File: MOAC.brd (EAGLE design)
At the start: 113 x 40 mm, 56 parts, among them IC1 ATMEGA32U4NT-TQFP, J1 3.5mm, J2 3.5mm, J3 3.5mm, J4 3.5mm, J5 3.5mm, J6 3.5mm, J7 3.5mm, J8 3.5mm, J9 USB-C

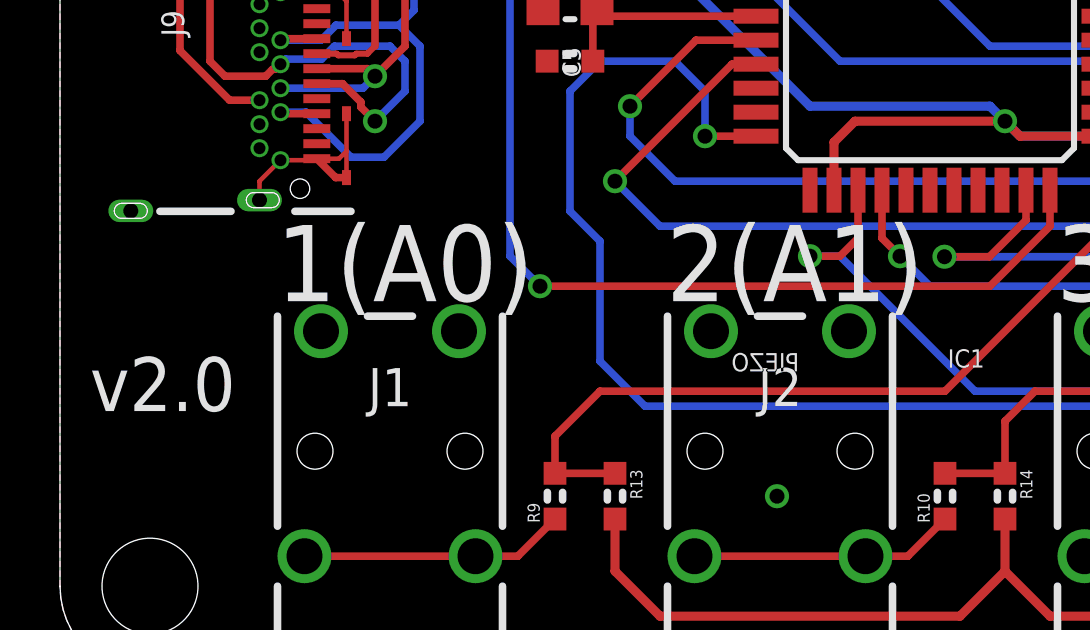
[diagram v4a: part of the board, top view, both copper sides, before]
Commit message: Changed button 8 from A11 to A7, to fix Jon's silly mistake from way back in v1.0
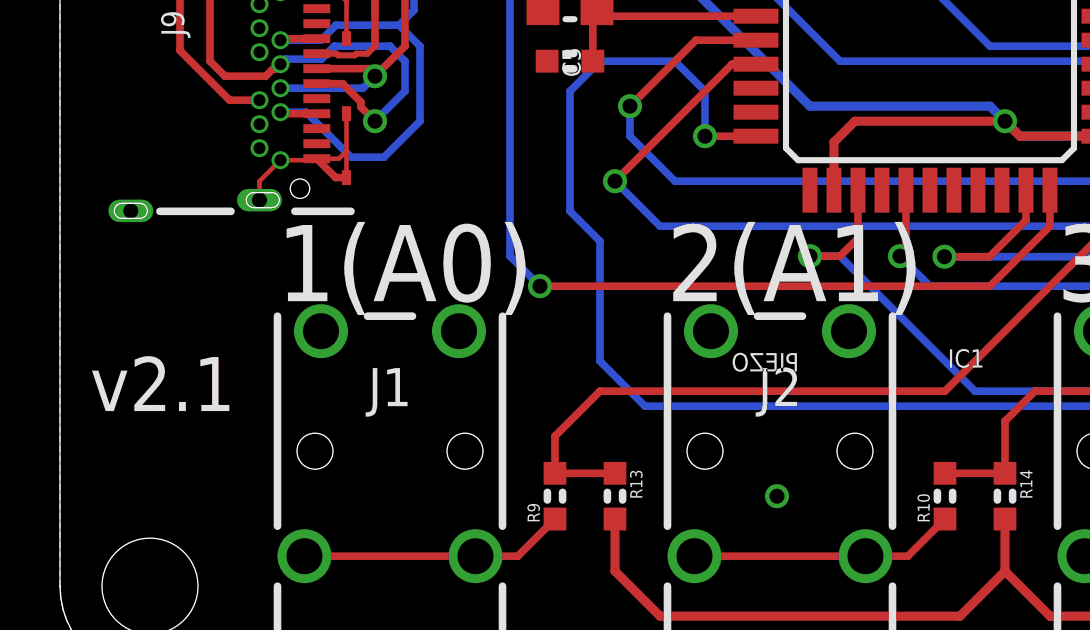
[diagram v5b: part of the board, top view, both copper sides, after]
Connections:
- net D10_A11 renamed D10_A10
- net D8_A9 renamed D8_A8
- net D9_A10 renamed D9_A9
- removed net D12_A7: IC1.26, R21.2, R25.1
- removed net D6_A8: IC1.27
- new net D12_A11: IC1.26
- new net D6_A7: IC1.27, R21.2, R25.1
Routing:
- net D12_A7: track 87.6 -> 0.00 mm, vias 2 -> 0
- net D6_A7: track 0.00 -> 87.4 mm, vias 0 -> 2
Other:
- board text added: "v2.1"
- board text removed: "v2.0"
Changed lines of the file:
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@@
 <drawing>
 <settings>
-<setting alwaysvectorfont="yes"/>
+<setting alwaysvectorfont="no"/>
 <setting keepoldvectorfont="yes"/>
 <setting verticaltext="up"/>
 </settings>
-<grid distance="1" unitdist="mm" unit="mm" style="dots" multiple="1" display="yes" altdistance="0.001" altunitdist="inch" altunit="inch"/>
+<grid distance="0.5" unitdist="mm" unit="mm" style="dots" multiple="1" display="yes" altdistance="0.001" altunitdist="inch" altunit="inch"/>
 <layers>
 <layer number="1" name="Top" color="4" fill="1" visible="yes" active="yes"/>
@@
 <layer number="20" name="Dimension" color="15" fill="1" visible="yes" active="yes"/>
 <layer number="21" name="tPlace" color="7" fill="1" visible="yes" active="yes"/>
-<layer number="22" name="bPlace" color="14" fill="1" visible="yes" active="yes"/>
+<layer number="22" name="bPlace" color="14" fill="1" visible="no" active="yes"/>
 <layer number="23" name="tOrigins" color="15" fill="1" visible="yes" active="yes"/>
 <layer number="24" name="bOrigins" color="15" fill="1" visible="yes" active="yes"/>
@@
 </layers>
 <board>
-<fusionsync huburn="a.cGVyc29uYWw6dWUyZDliZmNi" projecturn="a.cGVyc29uYWw6dWUyZDliZmNiIzIwMTgxMTA5MTU5MjczMjgx" f3durn="urn:adsk.wipprod:dm.lineage:ugFpkX5gRSuWYfeIfJSr2A" pcbguid="4ef23d0d-506b-4405-99bc-0b8b5e44c8a7" lastpulledtime="" lastsyncedchangeguid="f2f5a112-46de-bc3b-63a8-23ca9d30e68b"/>
+<fusionsync huburn="a.cGVyc29uYWw6dWUyZDliZmNi" projecturn="a.cGVyc29uYWw6dWUyZDliZmNiIzIwMTgxMTA5MTU5MjczMjgx" f3durn="urn:adsk.wipprod:dm.lineage:ugFpkX5gRSuWYfeIfJSr2A" pcbguid="4ef23d0d-506b-4405-99bc-0b8b5e44c8a7" lastpulledtime="" lastsyncedchangeguid="1a155890-40f8-0c29-352a-23eae3b4c9ee"/>
 <plain>
 <wire x1="113" y1="3" x2="113" y2="37" width="0" layer="20"/>
@@
 <text x="44.958" y="14.224" size="0.6096" layer="25">LED1</text>
 <text x="44.958" y="4.572" size="0.6096" layer="25">LED2</text>
-<text x="1" y="8.8364" size="1.8" layer="21" font="vector" ratio="15">v2.0</text>
+<text x="1" y="8.8364" size="1.8" layer="21" font="vector" ratio="15">v2.1</text>
 <hole x="3" y="3" drill="3.2"/>
 <hole x="3" y="37" drill="3.2"/>
@@
 <element name="C2" library="SuperHouse-DiscreteSemi" library_urn="urn:adsk.eagle:library:11768461" package="C0603" package3d_urn="urn:adsk.eagle:package:7066315/6" value="100nF" x="37" y="30" smashed="yes" rot="R270">
 <attribute name="NAME" x="37.4826" y="30.2794" size="0.6096" layer="25" font="vector" rot="R180"/>
-<attribute name="VALUE" x="35.984" y="31.357" size="0.8128" layer="27" font="vector"/>
+<attribute name="VALUE" x="37.984" y="29.357" size="0.8128" layer="27" font="vector"/>
 </element>
 <element name="R2" library="SuperHouse-DiscreteSemi" library_urn="urn:adsk.eagle:library:11768461" package="R0603" package3d_urn="urn:adsk.eagle:package:11768543/2" value="10K" x="20.5" y="27" smashed="yes" rot="R270">
 <attribute name="NAME" x="20.9064" y="27.2793" size="0.6096" layer="25" font="vector" rot="R180"/>
-<attribute name="VALUE" x="20.1431" y="25.984" size="0.8128" layer="27" font="vector" rot="R90"/>
+<attribute name="VALUE" x="17.984" y="27.8569" size="0.8128" layer="27" font="vector"/>
 </element>
 <element name="C3" library="SuperHouse-DiscreteSemi" library_urn="urn:adsk.eagle:library:11768461" package="C0603" package3d_urn="urn:adsk.eagle:package:7066315/6" value="1uF" x="12" y="34" smashed="yes" rot="R180">
@@
 <element name="C1" library="SuperHouse-DiscreteSemi" library_urn="urn:adsk.eagle:library:11768461" package="C0603" package3d_urn="urn:adsk.eagle:package:7066315/6" value="100nF" x="37" y="26" smashed="yes" rot="R90">
 <attribute name="NAME" x="36.5174" y="25.7206" size="0.6096" layer="25" font="vector"/>
-<attribute name="VALUE" x="36.484" y="23.857" size="0.8128" layer="27" font="vector"/>
+<attribute name="VALUE" x="37.484" y="26.857" size="0.8128" layer="27" font="vector"/>
 </element>
 <element name="ICSP" library="SuperHouse-Connectors" library_urn="urn:adsk.eagle:library:11765989" package="2X03PTH" package3d_urn="urn:adsk.eagle:package:11765966/5" value="ICSP" x="32.7036" y="36.64" smashed="yes">
@@
 <element name="Z2" library="SuperHouse-DiscreteSemi" library_urn="urn:adsk.eagle:library:11768461" package="TVS0603" package3d_urn="urn:adsk.eagle:package:11801346/2" value="PGB1010603" x="28.5" y="31" smashed="yes" rot="R90">
 <attribute name="NAME" x="28.754" y="30.619" size="0.4064" layer="25" font="vector" rot="R90"/>
-<attribute name="VALUE" x="28.4652" y="32.484" size="0.8128" layer="27" font="vector" rot="R90"/>
+<attribute name="VALUE" x="27.9652" y="28.984" size="0.8128" layer="27" font="vector" rot="R90"/>
 </element>
 <element name="C5" library="SuperHouse-DiscreteSemi" library_urn="urn:adsk.eagle:library:11768461" package="C0603" package3d_urn="urn:adsk.eagle:package:7066315/6" value="15pF" x="17" y="20.5" smashed="yes">
@@
 <element name="C4" library="SuperHouse-DiscreteSemi" library_urn="urn:adsk.eagle:library:11768461" package="C0603" package3d_urn="urn:adsk.eagle:package:7066315/6" value="1uF" x="25.5" y="31" smashed="yes" rot="R270">
 <attribute name="NAME" x="24.9666" y="30.7206" size="0.6096" layer="25" font="vector"/>
-<attribute name="VALUE" x="24.484" y="30.5348" size="0.8128" layer="27" font="vector"/>
+<attribute name="VALUE" x="23.984" y="30.5348" size="0.8128" layer="27" font="vector"/>
 </element>
 <element name="XTL1" library="SuperHouse-Oscillators" library_urn="urn:adsk.eagle:library:11786724" package="CRYSTAL-SMD-3X2" package3d_urn="urn:adsk.eagle:package:7066259/2" value="16MHz" x="17" y="23.5" smashed="yes" rot="R270">
@@
 <element name="R1" library="SuperHouse-DiscreteSemi" library_urn="urn:adsk.eagle:library:11768461" package="R0603" package3d_urn="urn:adsk.eagle:package:11768543/2" value="22R" x="32.5" y="31" smashed="yes" rot="R270">
 <attribute name="NAME" x="33.008" y="31.889" size="0.4064" layer="25" font="vector" rot="R270"/>
-<attribute name="VALUE" x="31.484" y="32.5348" size="0.8128" layer="27" font="vector"/>
+<attribute name="VALUE" x="31.484" y="30.5348" size="0.8128" layer="27" font="vector"/>
 </element>
 <element name="R6" library="SuperHouse-DiscreteSemi" library_urn="urn:adsk.eagle:library:11768461" package="R0603" package3d_urn="urn:adsk.eagle:package:11768543/2" value="22R" x="30.5" y="31" smashed="yes" rot="R270">
 <attribute name="NAME" x="31.008" y="31.889" size="0.4064" layer="25" font="vector" rot="R270"/>
-<attribute name="VALUE" x="29.484" y="30.5348" size="0.8128" layer="27" font="vector"/>
+<attribute name="VALUE" x="29.484" y="32.0348" size="0.8128" layer="27" font="vector"/>
 </element>
 <element name="S10" library="SuperHouse-Switches" library_urn="urn:adsk.eagle:library:11744182" package="TACTILE_SMD_3X4X2" package3d_urn="urn:adsk.eagle:package:11818379/3" value="HWB" x="9" y="37" smashed="yes" rot="R180"/>
@@
 <attribute name="VALUE" x="47.28" y="22.215" size="1.27" layer="27"/>
 </element>
-<element name="IC1" library="SuperHouse-MCUs" library_urn="urn:adsk.eagle:library:11815114" package="TQFP44" package3d_urn="urn:adsk.eagle:package:12190647/2" value="ATMEGA32U4NT-TQFP" x="29" y="22" smashed="yes" rot="R270">
+<element name="IC1" library="SuperHouse-MCUs" library_urn="urn:adsk.eagle:library:11815114" package="TQFP44" package3d_urn="urn:adsk.eagle:package:12190647/3" value="ATMEGA32U4NT-TQFP" x="29" y="22" smashed="yes" rot="R270">
 <attribute name="NAME" x="35.985" y="25.81" size="1.778" layer="25" rot="R270"/>
-<attribute name="VALUE" x="20.2449" y="26.445" size="1.778" layer="27" rot="R270"/>
+<attribute name="VALUE" x="24.555" y="19.2449" size="0.8128" layer="27"/>
 </element>
 </elements>
@@
 <wire x1="106.762" y1="25" x2="109.238" y2="25" width="0.254" layer="1"/>
 </signal>
-<signal name="D12_A7">
-<contactref element="R21" pad="2"/>
-<contactref element="R25" pad="1"/>
-<wire x1="109.5" y1="9.762" x2="107.5" y2="9.762" width="0.254" layer="1"/>
-<via x="28" y="14" extent="1-16" drill="0.5"/>
-<wire x1="28" y1="14" x2="29" y2="13" width="0.254" layer="16"/>
-<via x="107.5" y="13" extent="1-16" drill="0.5"/>
-<wire x1="107.5" y1="13" x2="107.5" y2="9.762" width="0.254" layer="1"/>
-<wire x1="29" y1="13" x2="107.5" y2="13" width="0.254" layer="16"/>
-<contactref element="IC1" pad="26"/>
-<wire x1="27.4" y1="16.2" x2="27.4" y2="14.6" width="0.254" layer="1"/>
-<wire x1="27.4" y1="14.6" x2="28" y2="14" width="0.254" layer="1"/>
-</signal>
 <signal name="D4_A6">
 <contactref element="R20" pad="2"/>
@@
 <contactref element="IC1" pad="21"/>
 </signal>
-<signal name="D6_A8">
+<signal name="D6_A7">
 <contactref element="IC1" pad="27"/>
-</signal>
-<signal name="D8_A9">
+<contactref element="R21" pad="2"/>
+<contactref element="R25" pad="1"/>
+<wire x1="109.5" y1="9.762" x2="107.5" y2="9.762" width="0.254" layer="1"/>
+<via x="28" y="14" extent="1-16" drill="0.5"/>
+<wire x1="28" y1="14" x2="29" y2="13" width="0.254" layer="16"/>
+<via x="107.5" y="13" extent="1-16" drill="0.5"/>
+<wire x1="107.5" y1="13" x2="107.5" y2="9.762" width="0.254" layer="1"/>
+<wire x1="29" y1="13" x2="107.5" y2="13" width="0.254" layer="16"/>
+<wire x1="28.2" y1="16.2" x2="28.2" y2="14.2" width="0.254" layer="1"/>
+<wire x1="28.2" y1="14.2" x2="28" y2="14" width="0.254" layer="1"/>
+</signal>
+<signal name="D8_A8">
 <contactref element="IC1" pad="28"/>
 </signal>
-<signal name="D9_A10">
+<signal name="D9_A9">
 <contactref element="IC1" pad="29"/>
 </signal>
-<signal name="D10_A11">
+<signal name="D10_A10">
 <contactref element="IC1" pad="30"/>
 </signal>
+<signal name="D12_A11">
+<contactref element="IC1" pad="26"/>
+</signal>
 </signals>

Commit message: Changed display from 128x32 to 128x64
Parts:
- MOD2: value OLED-I2C128X64-1.3-HO -> OLED-I2C128X64-1.3-5.08; device SuperHouse-Displays:OLED-128X64-1.3-HO -> SuperHouse-Displays:OLED-128X64-1.3-5.08
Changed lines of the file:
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@@
 <?xml version="1.0" encoding="utf-8"?>
 <!DOCTYPE eagle SYSTEM "eagle.dtd">
-<eagle version="9.4.2">
+<eagle version="9.5.2">
 <drawing>
 <settings>
@@
 </layers>
 <board>
-<fusionsync huburn="a.cGVyc29uYWw6dWUyZDliZmNi" projecturn="a.cGVyc29uYWw6dWUyZDliZmNiIzIwMTgxMTA5MTU5MjczMjgx" f3durn="urn:adsk.wipprod:dm.lineage:ugFpkX5gRSuWYfeIfJSr2A" pcbguid="4ef23d0d-506b-4405-99bc-0b8b5e44c8a7" lastpulledtime="" lastsyncedchangeguid="1a155890-40f8-0c29-352a-23eae3b4c9ee"/>
+<fusionsync huburn="a.cGVyc29uYWw6dWUyZDliZmNi" projecturn="a.cGVyc29uYWw6dWUyZDliZmNiIzIwMTgxMTA5MTU5MjczMjgx" f3durn="urn:adsk.wipprod:dm.lineage:ugFpkX5gRSuWYfeIfJSr2A" pcbguid="4ef23d0d-506b-4405-99bc-0b8b5e44c8a7" lastpulledtime="" lastsyncedchangeguid="8fe81872-e2fd-63fb-760c-4497a8ebff07"/>
 <plain>
 <wire x1="113" y1="3" x2="113" y2="37" width="0" layer="20"/>
@@
 <attribute name="VALUE" x="17.984" y="7.5348" size="0.8128" layer="27" font="vector"/>
 </element>
-<element name="MOD2" library="SuperHouse-Displays" library_urn="urn:adsk.eagle:library:11966779" package="OLED-128X64-1.3-HO" package3d_urn="urn:adsk.eagle:package:12058301/2" value="OLED-I2C128X64-1.3-HO" x="56.5" y="20" smashed="yes">
+<element name="MOD2" library="SuperHouse-Displays" library_urn="urn:adsk.eagle:library:11966779" package="OLED-128X64-1.3-5.08" package3d_urn="urn:adsk.eagle:package:16152188/2" value="OLED-I2C128X64-1.3-5.08" x="56.5" y="20" smashed="yes">
 <attribute name="NAME" x="47.2038" y="31.1788" size="1.27" layer="25" ratio="10"/>
 <attribute name="VALUE" x="47.28" y="22.215" size="1.27" layer="27"/>

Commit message: Added piezo switch; replaced USB-C socket for v2.1 release
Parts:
- removed J9: USB-C, SuperHouse-Connectors:USB-C-U52A
- removed SJ2: SND, SuperHouse-Jumpers:SJC
- added J10: USB-C-16P-16P, SuperHouse-Connectors:USB-C-16P
- added SW1: SWITCH-SPDT-4TABSSMT, SuperHouse-Switches:MK-12C02
- C3: device SuperHouse-DiscreteSemi:C0603 -> SuperHouse-DiscreteSemi:C0805
- moved R7 15.5 mm to (9.50, 16.5), turned to 90 degrees
- moved R18 10.6 mm to (9.50, 23.5)
- moved C3 3.04 mm to (12.5, 31.0), turned to 270 degrees
- moved F1 2.50 mm to (7.50, 31.0)
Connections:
- removed net N$67: J9.A5, R7.2
- new net N$17: J10.A5, R18.2
- net D+: now also J10.A6, J10.B6; no longer J9.A6, J9.B6
- net D-: now also J10.A7, J10.B7; no longer J9.A7, J9.B7
- net D11: now also SW1.2; no longer SJ2.2
- net GND: now also J10.A12B1, J10.A1B12, J10.FIX1, J10.FIX2, J10.FIX3, J10.FIX4, SW1.MNT@1, SW1.MNT@2, SW1.MNT@3, SW1.MNT@4; no longer J9.A1, J9.A12, J9.B1, J9.B12, J9.CASE1, J9.CASE2, J9.CASE3, J9.CASE4, J9.FIX1, J9.FIX2, J9.FIX3, J9.FIX4
- net N$1: now also J10.B5, R7.2; no longer J9.B5, R18.2
- net N$16: now also SW1.1; no longer SJ2.1
- net USB+: now also J10.A4B9, J10.A9B4; no longer J9.A4, J9.A9, J9.B4, J9.B9
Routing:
- net D11: track 66.4 -> 95.5 mm
- net N$16: track 3.24 -> 27.3 mm
- net N$67: track 15.5 -> 0.00 mm, vias 2 -> 0
- net GND: track 13.3 -> 0.00 mm, vias 4 -> 6
- net D-: track 51.4 -> 38.5 mm, vias 1 -> 0
- net N$1: track 13.5 -> 2.81 mm
- net USB+: track 38.0 -> 27.7 mm
- net RXLED_SS: track 85.0 -> 93.5 mm
- net D+: track 32.9 -> 37.0 mm, vias 1 -> 2
- net N$17: track 0.00 -> 3.45 mm
- net 5V: track 344.3 -> 345.8 mm
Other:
- board text added: "BEEP"

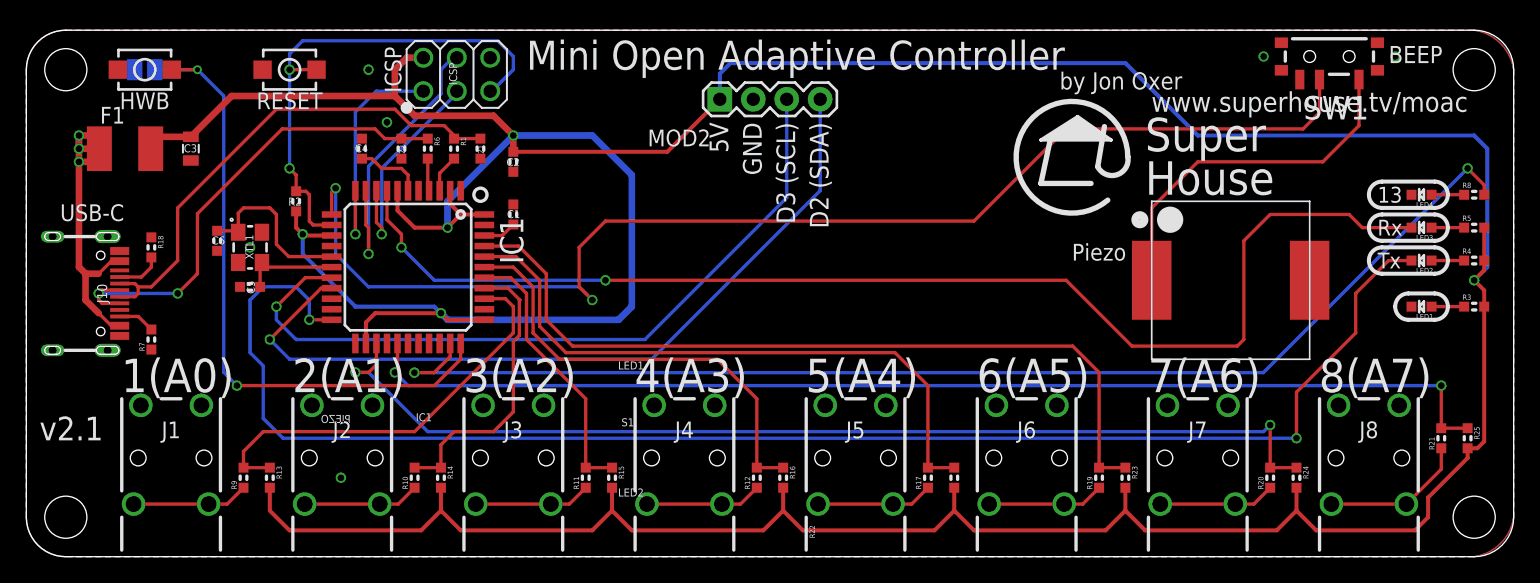
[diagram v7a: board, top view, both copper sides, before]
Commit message: Final tweaks and DRC for v2.1 release
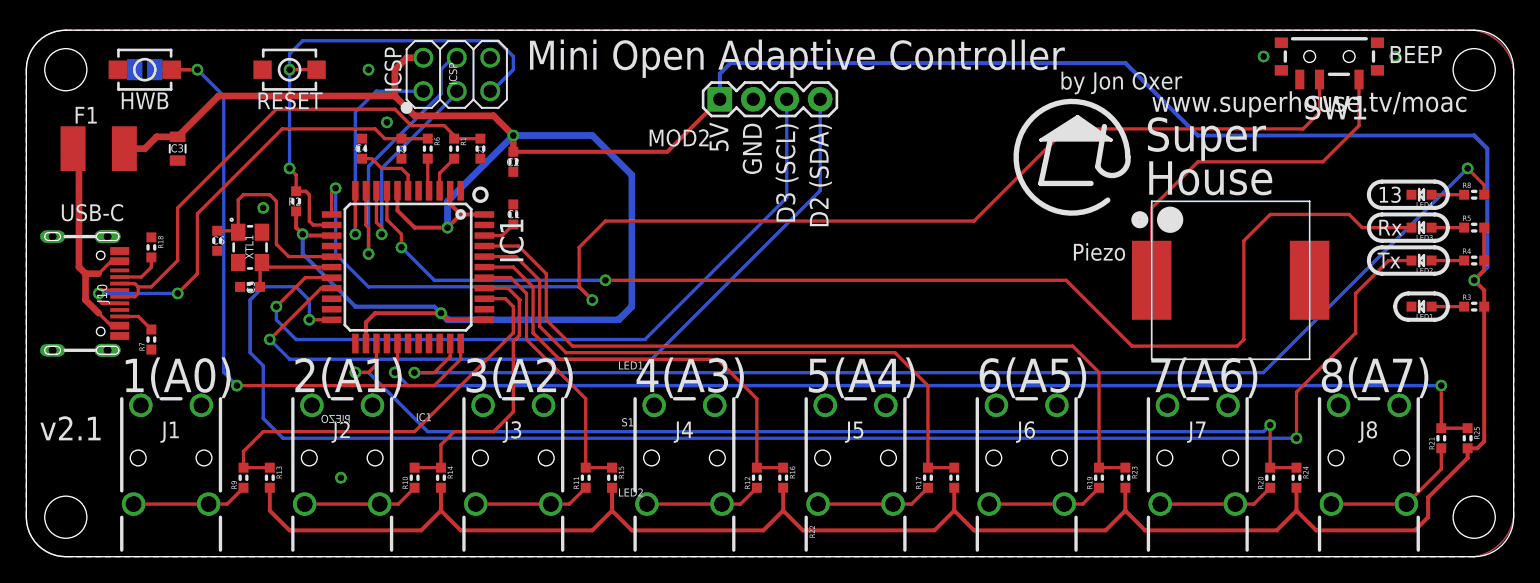
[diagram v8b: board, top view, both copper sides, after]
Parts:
- moved F1 2.00 mm to (5.50, 31.0)
- moved C3 1.00 mm to (11.5, 31.0)
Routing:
- net USB+: track 27.7 -> 18.3 mm, vias 3 -> 0
- net N$12: track 13.6 -> 15.6 mm
- net 5V: track 345.8 -> 347.5 mm
